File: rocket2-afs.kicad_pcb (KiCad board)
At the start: 4 copper layers, 70 x 50 mm, 67 parts, among them J1 ARMING_PLUG, J2 POWER, J3 E-MATCH_DROGUE, J4 SWD, J5 E-MATCH_RECOVERY, Q1 Q_NMOS_GSD, Q2 Q_NMOS_GSD, Q3 Q_NMOS_GSD, Q4 Q_NMOS_GSD, Q5 Q_NMOS_GSD, U2 LD1086DT33TR, U8 USBLC6-2SC6, Y1 16MHz

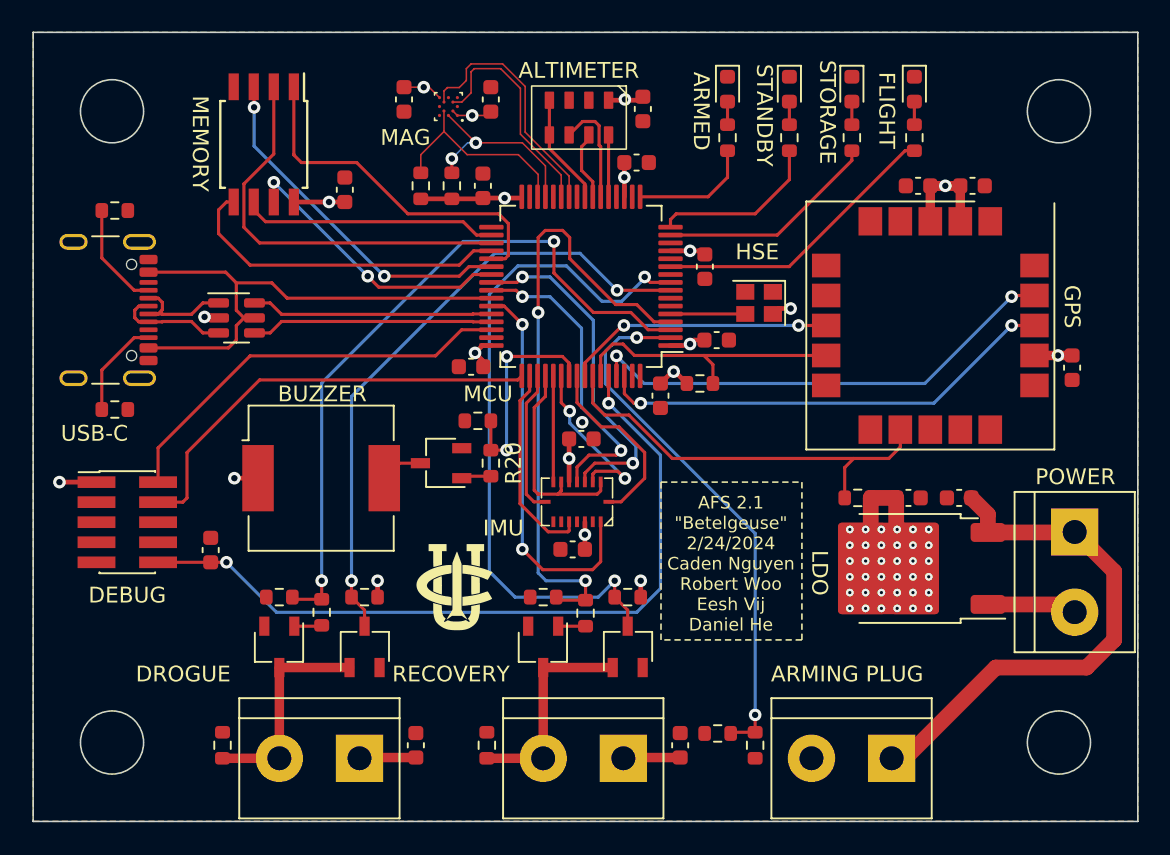
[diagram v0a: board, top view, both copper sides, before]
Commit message: Completely Remade PCB to adjust for GPS GND Shield
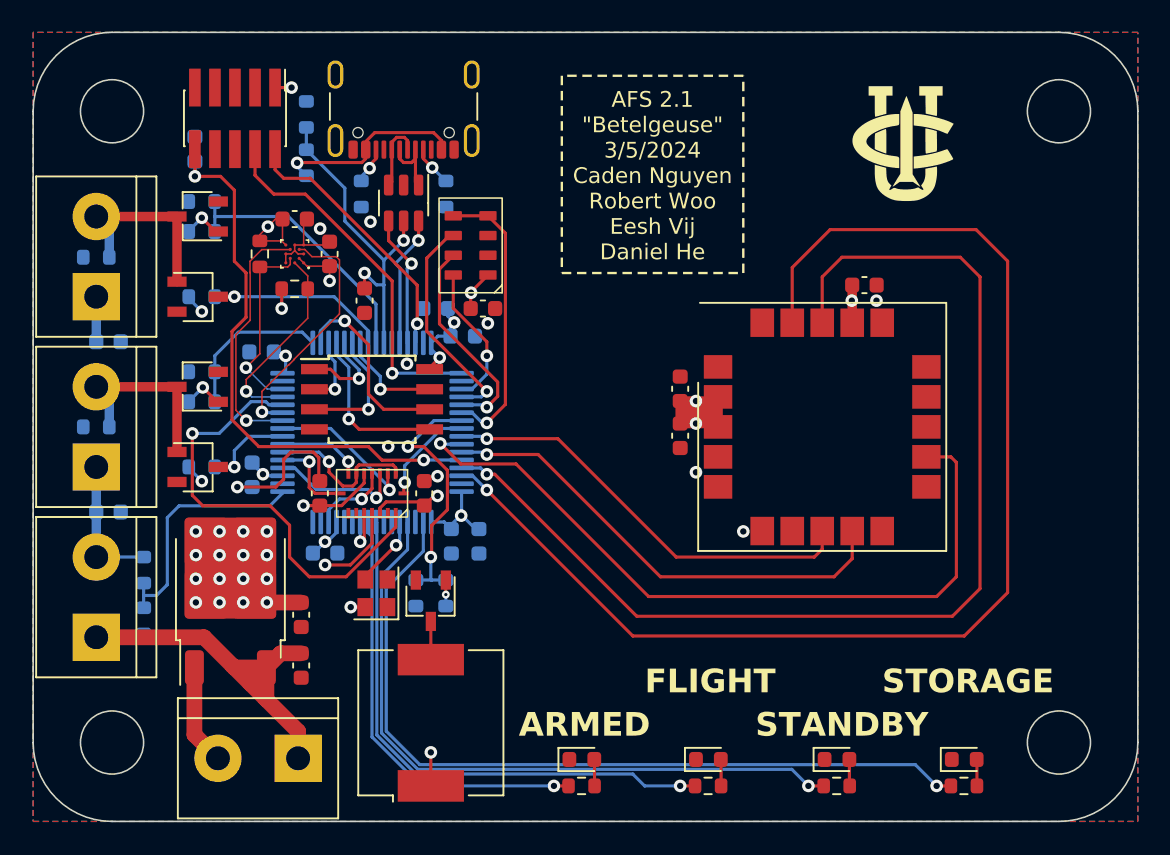
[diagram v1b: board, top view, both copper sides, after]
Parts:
- added C21: 4.7uF, Capacitor_SMD:C_0603_1608Metric, F.Cu at (141.0, 77.0)
- C1, C11, C12, C2, C3, C4, C5, C6, C7, C8, R1, R12, R15, R16, R19, R2, R20, R21, R22, R3, U1: moved to B.Cu
- R11, R4: value 1k -> 10k; moved to B.Cu
- R13: value 4k7 -> 33k; moved to B.Cu
- R14: value 4k7 -> 82k; moved to B.Cu
- R5, R8: value 100k -> 10k; moved to B.Cu
- moved J2 51.3 mm to (136.8, 106.0), turned to 180 degrees
- moved J1 51.0 mm to (124.0, 98.3), turned to 90 degrees
- moved D2 44.4 mm to (162.8, 106.1), turned to 0 degrees
- moved D1 43.5 mm to (154.8, 106.1), turned to 0 degrees
- moved R7 43.1 mm to (162.8, 107.8), turned to 0 degrees
- moved D4 43.1 mm to (179.0, 106.1), turned to 0 degrees
- moved C9 43.0 mm to (137.0, 100.1), turned to 90 degrees
- moved U2 43.0 mm to (132.5, 95.2), turned to 90 degrees
- moved D3 42.6 mm to (170.9, 106.1), turned to 0 degrees
- moved R6 42.1 mm to (154.8, 107.8), turned to 0 degrees
- moved R10 41.7 mm to (179.0, 107.8), turned to 0 degrees
- moved R9 41.2 mm to (170.9, 107.8), turned to 0 degrees
- moved R13 40.9 mm to (137.3, 68.3), turned to 90 degrees
- moved R1 40.3 mm to (127.0, 94.1), turned to -90 degrees
- moved C10 39.2 mm to (137.0, 96.9), turned to 90 degrees
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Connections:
- J6 pad A4: VBUS -> Net-(J6-VBUS-PadA4)
- J6 pad A9: VBUS -> Net-(J6-VBUS-PadA4)
- J6 pad B4: VBUS -> Net-(J6-VBUS-PadA4)
- J6 pad B9: VBUS -> Net-(J6-VBUS-PadA4)
- R13 pad 1: +3.3V -> Net-(J6-VBUS-PadA4)
- R13 pad 2: GPS_SCL -> VBUS
- R14 pad 1: +3.3V -> GND
- R14 pad 2: GPS_SDA -> VBUS
- U1 pad 10: unconnected-(U1-PC2-Pad10) -> IMU_CS2
- U1 pad 11: LED_FLIGHT -> unconnected-(U1-PC3-Pad11)
- U1 pad 14: unconnected-(U1-PA0-Pad14) -> IMU_INT3
- U1 pad 15: LED_STORAGE -> unconnected-(U1-PA1-Pad15)
- U1 pad 16: LED_STANDBY -> unconnected-(U1-PA2-Pad16)
- U1 pad 17: LED_ARMED -> ARM_CONT
- U1 pad 2: ARM_CONT -> LED_STORAGE
- U1 pad 20: unconnected-(U1-PA4-Pad20) -> IMU_INT4
- U1 pad 21: ALT_SCK -> IMU_SCK
- U1 pad 22: ALT_MISO -> IMU_MISO
- U1 pad 23: ALT_MOSI -> IMU_MOSI
- U1 pad 24: ALT_CS -> RECOVERY_CONT
- U1 pad 25: unconnected-(U1-PC5-Pad25) -> IMU_CS1
- U1 pad 28: unconnected-(U1-PB2-Pad28) -> IMU_INT2
- U1 pad 3: DROGUE -> unconnected-(U1-PC14-Pad3)
- U1 pad 33: unconnected-(U1-PB12-Pad33) -> RECOVERY
- U1 pad 4: RECOVERY -> LED_STANDBY
- U1 pad 40: IMU_INT4 -> DROGUE_CONT
- U1 pad 41: IMU_INT3 -> DROGUE
- U1 pad 43: IMU_INT2 -> unconnected-(U1-PA10-Pad43)
- U1 pad 50: IMU_CS2 -> unconnected-(U1-PA15-Pad50)
- U1 pad 51: IMU_SCK -> ALT_SCK
- U1 pad 52: IMU_MISO -> ALT_MISO
- U1 pad 53: IMU_MOSI -> ALT_MOSI
- U1 pad 54: IMU_CS1 -> ALT_CS
- U1 pad 61: GPS_INT -> GPS_RESET
- U1 pad 62: GPS_RESET -> GPS_INT
- U1 pad 8: DROGUE_CONT -> LED_FLIGHT
- U1 pad 9: RECOVERY_CONT -> LED_ARMED
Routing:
- net GPS_INT: track 30.8 -> 79.9 mm, vias 2 -> 1
- net GPS_RESET: track 29.4 -> 71.2 mm, vias 2 -> 1
- net LED_STORAGE: track 14.1 -> 51.7 mm, vias 0 -> 1
- net RECOVERY_CONT: track 43.8 -> 6.49 mm, vias 2 -> 1
- net LED_STANDBY: track 10.9 -> 43.5 mm, vias 0 -> 1
- net RECOVERY: track 39.4 -> 10.0 mm, vias 2 -> 0
- net DROGUE: track 45.1 -> 16.9 mm, vias 2 -> 0
- net DROGUE_CONT: track 39.8 -> 12.4 mm, vias 2 -> 1
- net MEM_MISO: track 25.8 -> 4.41 mm, vias 0 -> 1
- net GPS_SCL: track 26.5 -> 47.9 mm, vias 0 -> 1
- net GND: track 6.75 -> 26.5 mm, vias 2 -> 11
- net LED_ARMED: track 7.74 -> 27.5 mm, vias 0 -> 1
- net ARM_CONT: track 34.1 -> 15.6 mm, vias 2 -> 0
- net MEM_CS: track 22.9 -> 5.72 mm, vias 0 -> 1
- net LED_FLIGHT: track 18.5 -> 35.0 mm, vias 0 -> 1
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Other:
- outline, holes or cut-outs redrawn
- board text added: "AFS 2.1 {dblquote}Betelgeuse{dblquote} 3/5/2024 Caden Nguyen Robert Woo Eesh Vij Daniel He"
- board text added: "ARM PLUG"
- board text added: "SWD"
- board text added: "USB"
- board text removed: "AFS 2.1 {dblquote}Betelgeuse{dblquote} 2/24/2024 Caden Nguyen Robert Woo Eesh Vij Daniel He"
- board text removed: "ARMING PLUG"
- board text removed: "DEBUG"
- board text removed: "HSE"
- board text removed: "LDO"
- board text removed: "USB-C"

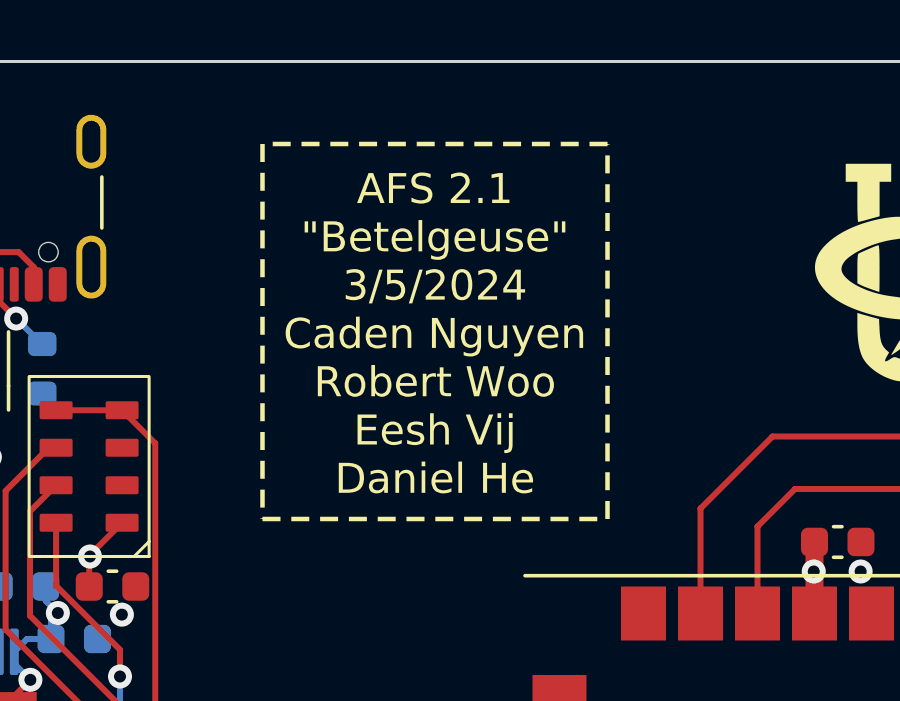
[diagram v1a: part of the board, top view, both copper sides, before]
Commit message: Silkscreen Changes for Readability
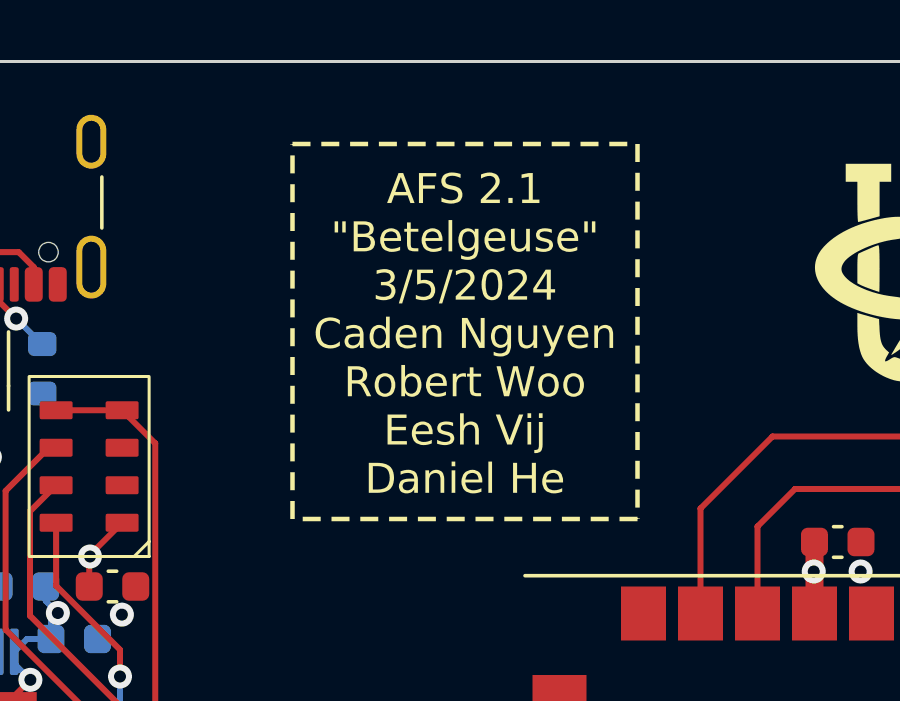
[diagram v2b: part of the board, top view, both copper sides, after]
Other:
- board text added: "IMU (F)"
- board text added: "MCU (B)"
- board text added: "MEMORY (F)"
- board text removed: "IMU"
- board text removed: "MCU"
- board text removed: "MEMORY"
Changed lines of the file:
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@@
     (property "Sheetname" "")
     (attr smd)
-    (fp_text reference "U1" (at 0 7.4 90) (layer "B.SilkS")
+    (fp_text reference "U1" (at 0 7.4 90) (layer "B.Fab")
         (effects (font (size 1 1) (thickness 0.15)) (justify mirror))
     )
@@
     )
     (stroke (width 0) (type solid)) (fill solid) (layer "F.SilkS"))
-  (gr_rect (start 153.5 75.25) (end 165 62.75)
+  (gr_rect (start 154.5 62.75) (end 166 75.25)
     (stroke (width 0.15) (type dash)) (fill none) (layer "F.SilkS"))
   (gr_rect (start 150 65) (end 190 105)
@@
     (effects (font (size 1 1) (thickness 0.25) bold) (justify left bottom mirror))
   )
-  (gr_text "ALTIMETER" (at 151.75 74.25) (layer "B.SilkS")
+  (gr_text "ALTIMETER" (at 153 74.25) (layer "B.SilkS")
     (effects (font (size 1 1) (thickness 0.25) bold) (justify left bottom mirror))
   )
@@
     (effects (font (size 1 1) (thickness 0.25) bold) (justify left bottom mirror))
   )
-  (gr_text "IMU" (at 153.25 87) (layer "B.SilkS")
+  (gr_text "IMU (F) " (at 156.071428 88) (layer "B.SilkS")
     (effects (font (size 1 1) (thickness 0.25) bold) (justify left bottom mirror))
   )
@@
     (effects (font (size 1 1) (thickness 0.25) bold) (justify left bottom mirror))
   )
-  (gr_text "MCU" (at 153.75 84) (layer "B.SilkS")
+  (gr_text "MCU (B) " (at 156.738095 83) (layer "B.SilkS")
     (effects (font (size 1 1) (thickness 0.25) bold) (justify left bottom mirror))
   )
-  (gr_text "MEMORY" (at 156.75 85.5) (layer "B.SilkS")
+  (gr_text "MEMORY (F) " (at 159.5 85.5) (layer "B.SilkS")
     (effects (font (size 1 1) (thickness 0.25) bold) (justify left bottom mirror))
   )
@@
     (effects (font (size 1.5 1.5) (thickness 0.3) bold) (justify left bottom))
   )
-  (gr_text "AFS 2.1\n{dblquote}Betelgeuse{dblquote}\n3/5/2024\nCaden Nguyen\nRobert Woo\nEesh Vij\nDaniel He" (at 159.25 74.5) (layer "F.SilkS")
+  (gr_text "AFS 2.1\n{dblquote}Betelgeuse{dblquote}\n3/5/2024\nCaden Nguyen\nRobert Woo\nEesh Vij\nDaniel He" (at 160.25 74.5) (layer "F.SilkS")
     (effects (font (size 1 1) (thickness 0.15)) (justify bottom))
   )

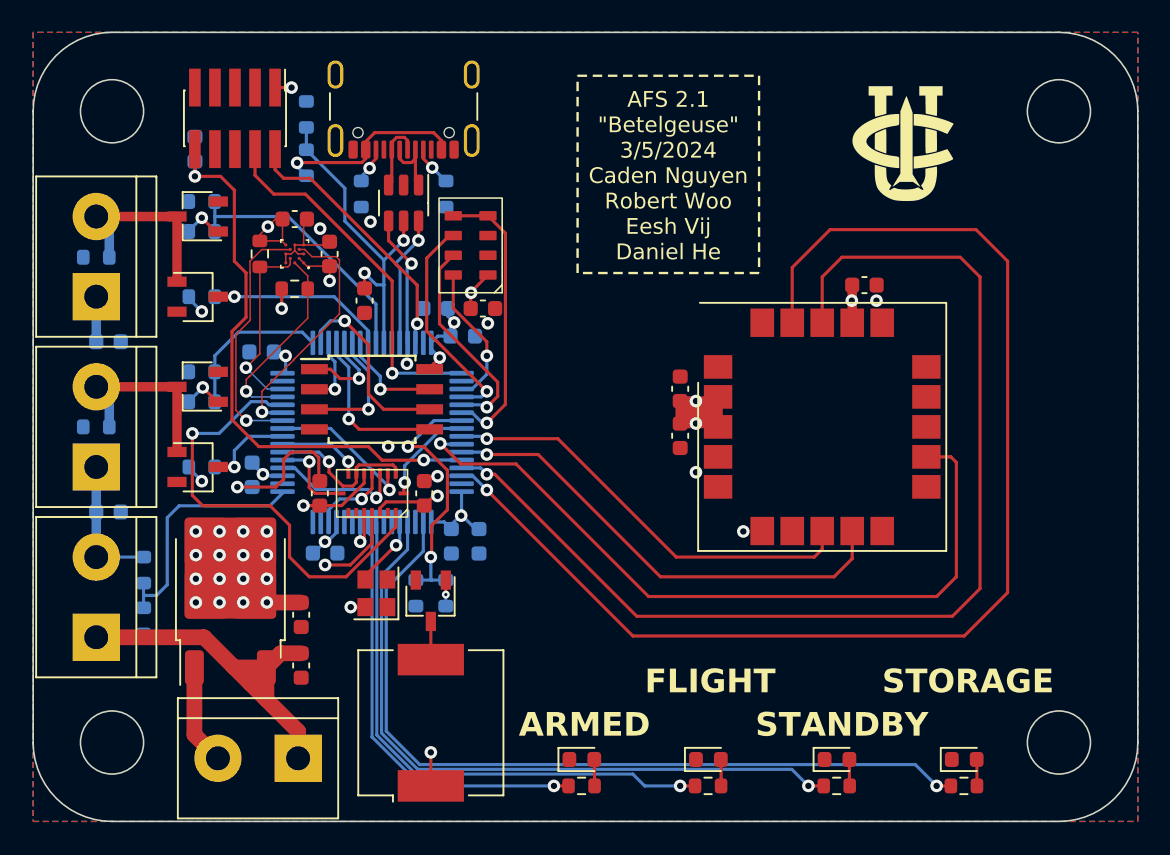
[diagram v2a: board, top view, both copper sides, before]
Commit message: Completely Remade PCB to Space out Components
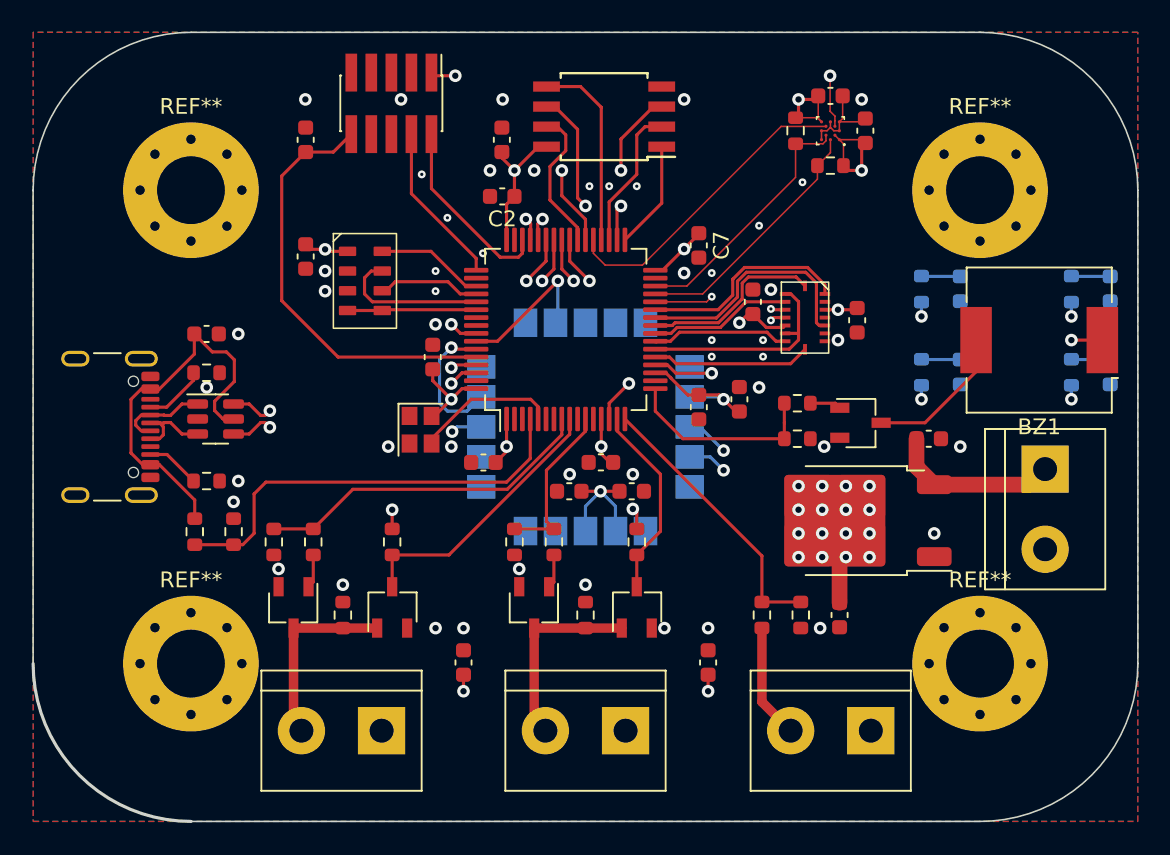
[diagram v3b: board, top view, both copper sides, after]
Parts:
- added REF**: MountingHole_4.3mm_M4_Pad_Via, MountingHole:MountingHole_4.3mm_M4_Pad_Via, F.Cu at (130.0, 100.0)
- added REF**: MountingHole_4.3mm_M4_Pad_Via, MountingHole:MountingHole_4.3mm_M4_Pad_Via, F.Cu at (130.0, 70.0)
- added REF**: MountingHole_4.3mm_M4_Pad_Via, MountingHole:MountingHole_4.3mm_M4_Pad_Via, F.Cu at (180.0, 100.0)
- added REF**: MountingHole_4.3mm_M4_Pad_Via, MountingHole:MountingHole_4.3mm_M4_Pad_Via, F.Cu at (180.0, 70.0)
- C1, C11, C12, C2, C3, C4, C5, C6, C7, C8, R1, R11, R12, R13, R14, R15, R16, R19, R2, R20, R21, R22, R3, R4, R5, R8, U1: moved to F.Cu
- D1, D2, D3, D4, R10, R6, R7, R9, U3: moved to B.Cu
- moved J2 50.8 mm to (184.1, 87.7), turned to -90 degrees
- moved J1 49.4 mm to (173.1, 104.2), turned to 180 degrees
- moved BZ1 45.5 mm to (183.8, 79.5), turned to 180 degrees
- moved C9 42.3 mm to (176.8, 85.8), turned to 180 degrees
- moved R2 41.6 mm to (168.6, 96.9)
- moved U2 39.8 mm to (172.1, 90.9), turned to 180 degrees
- moved R1 39.3 mm to (166.2, 96.9), turned to 90 degrees
- moved D2 39.2 mm to (188.2, 76.2), turned to 90 degrees
- moved C11 39.2 mm to (162.8, 99.9), turned to -90 degrees
- moved R7 39.0 mm to (185.8, 76.3), turned to 90 degrees
- moved D1 38.3 mm to (178.8, 76.2), turned to 90 degrees
- moved R6 38.1 mm to (176.3, 76.3), turned to 90 degrees
- moved J5 37.5 mm to (157.5, 104.2), turned to 180 degrees
- moved C19 36.6 mm to (172.7, 66.2), turned to 90 degrees
- moved C18 35.8 mm to (172.2, 78.2), turned to -90 degrees
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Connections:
- J6 pad A4: Net-(J6-VBUS-PadA4) -> VBUS
- J6 pad A9: Net-(J6-VBUS-PadA4) -> VBUS
- J6 pad B4: Net-(J6-VBUS-PadA4) -> VBUS
- J6 pad B9: Net-(J6-VBUS-PadA4) -> VBUS
- R13 pad 1: Net-(J6-VBUS-PadA4) -> VBUS
- R13 pad 2: VBUS -> VBUS_SENS
- R14 pad 2: VBUS -> VBUS_SENS
- U1 pad 10: IMU_CS2 -> unconnected-(U1-PC2-Pad10)
- U1 pad 11: unconnected-(U1-PC3-Pad11) -> RECOVERY
- U1 pad 15: unconnected-(U1-PA1-Pad15) -> RECOVERY_CONT
- U1 pad 16: unconnected-(U1-PA2-Pad16) -> ARM_CONT
- U1 pad 17: ARM_CONT -> BUZZER
- U1 pad 2: LED_STORAGE -> unconnected-(U1-PC13-Pad2)
- U1 pad 24: RECOVERY_CONT -> IMU_CS1
- U1 pad 25: IMU_CS1 -> IMU_INT1
- U1 pad 26: MAG_DRDY -> IMU_CS2
- U1 pad 27: MAG_INT -> IMU_INT2
- U1 pad 28: IMU_INT2 -> MAG_INT
- U1 pad 33: RECOVERY -> MEM_CS
- U1 pad 37: MEM_CS -> MAG_DRDY
- U1 pad 4: LED_STANDBY -> VBUS_SENS
- U1 pad 40: DROGUE_CONT -> LED_ARMED
- U1 pad 41: DROGUE -> LED_FLIGHT
- U1 pad 42: VBUS -> LED_STANDBY
- U1 pad 43: unconnected-(U1-PA10-Pad43) -> LED_STORAGE
- U1 pad 55: BUZZER -> unconnected-(U1-PB3-Pad55)
- U1 pad 56: IMU_INT1 -> unconnected-(U1-PB4-Pad56)
- U1 pad 8: LED_FLIGHT -> DROGUE
- U1 pad 9: LED_ARMED -> DROGUE_CONT
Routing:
- net GPS_INT: track 79.9 -> 23.9 mm, vias 1 -> 2
- net GPS_RESET: track 71.2 -> 23.8 mm, vias 1 -> 2
- net GPS_SCL: track 47.9 -> 9.47 mm
- net VBUS_SENS: track 0.00 -> 27.5 mm
- net USB_D+: track 8.36 -> 33.7 mm, vias 1 -> 2
- net USB_D-: track 8.43 -> 33.7 mm, vias 1 -> 2
- net GPS_SDA: track 30.4 -> 8.68 mm
- net GND: track 26.5 -> 6.25 mm, vias 11 -> 49
- net GPS_SAFEBOOT: track 27.4 -> 11.2 mm, vias 1 -> 2
- net IMU_INT2: track 28.9 -> 13.5 mm, vias 1 -> 0
- net VCC: track 25.2 -> 10.8 mm
- net DEBUCK_SWCLK: track 23.5 -> 10.3 mm, vias 1 -> 0
- net IMU_CS2: track 3.10 -> 16.0 mm, vias 1 -> 0
- net Net-(J6-VBUS-PadA4): track 11.9 -> 0.00 mm, vias 1 -> 0
- net IMU_INT3: track 5.04 -> 15.7 mm, vias 1 -> 2
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- added copper zone on In2.Cu, net VCC
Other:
- outline, holes or cut-outs redrawn
- board text removed: "AFS 2.1 {dblquote}Betelgeuse{dblquote} 3/5/2024 Caden Nguyen Robert Woo Eesh Vij Daniel He"
- board text removed: "ALTIMETER"
- board text removed: "ARM PLUG"
- board text removed: "ARMED"
- board text removed: "BUZZER"
- board text removed: "DROGUE"
- board text removed: "FLIGHT"
- board text removed: "GPS"
- board text removed: "IMU (F)"
- board text removed: "MAG"
- board text removed: "MCU (B)"
- board text removed: "MEMORY (F)"
- board text removed: "POWER"
- board text removed: "RECOVERY"
- board text removed: "STANDBY"
- board text removed: "STORAGE"
- board text removed: "SWD"
- board text removed: "USB"
